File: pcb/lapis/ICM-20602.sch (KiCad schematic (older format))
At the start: 5 parts, among them U2 ICM-20602

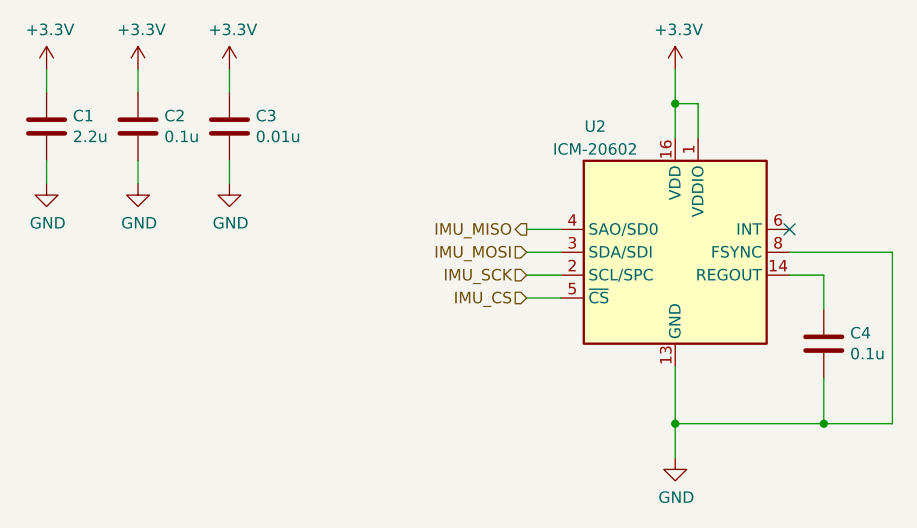
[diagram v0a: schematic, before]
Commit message: 信地旋回探索
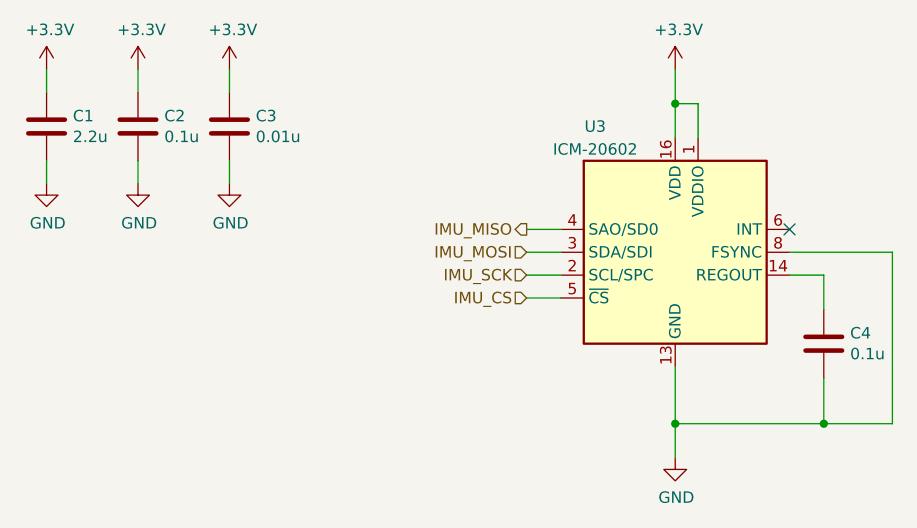
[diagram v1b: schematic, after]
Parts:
- renumbered U2 to U3
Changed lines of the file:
@@
 $Descr A4 11693 8268
 encoding utf-8
-Sheet 2 14
+Sheet 2 15
 Title ""
 Date ""
@@
 IMU_MOSI
 $Comp
-L Sensor_Motion:ICM-20602 U2
+L Sensor_Motion:ICM-20602 U3
 U 1 1 5FB362FC
 P 5850 4300
-F 0 "U2" H 5500 4850 50  0000 C CNN
+F 0 "U3" H 5500 4850 50  0000 C CNN
 F 1 "ICM-20602" H 5500 4750 50  0000 C CNN
 F 2 "Package_LGA:LGA-16_3x3mm_P0.5mm_LayoutBorder3x5y" H 5850 4550 50  0001 C CNN
